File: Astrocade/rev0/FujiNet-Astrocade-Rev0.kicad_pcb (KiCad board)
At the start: 4 copper layers, 96 x 58 mm, 95 parts, among them J1 Astrocade_Cart_Edge_26, J2 microSD, J3 USB-C, Q2 BC847C, Q3 BC847C, SW1 RESET, SW2 BOOTSEL, SW3 RESET, SW4 BOOT, U1 RP2040, U2 ESP32-S3-WROOM-1-N16R8, U3 CP2102N-A02-GQFN28, U4 UMH3N, U5 AP63203WU, U6 W25Q16JVSSIQ, U7 SN74LVC245APW(data), U8 SN74LVC245APW(addr-lo), U9 SN74LVC245APW(addr-hi), Y1 12MHz

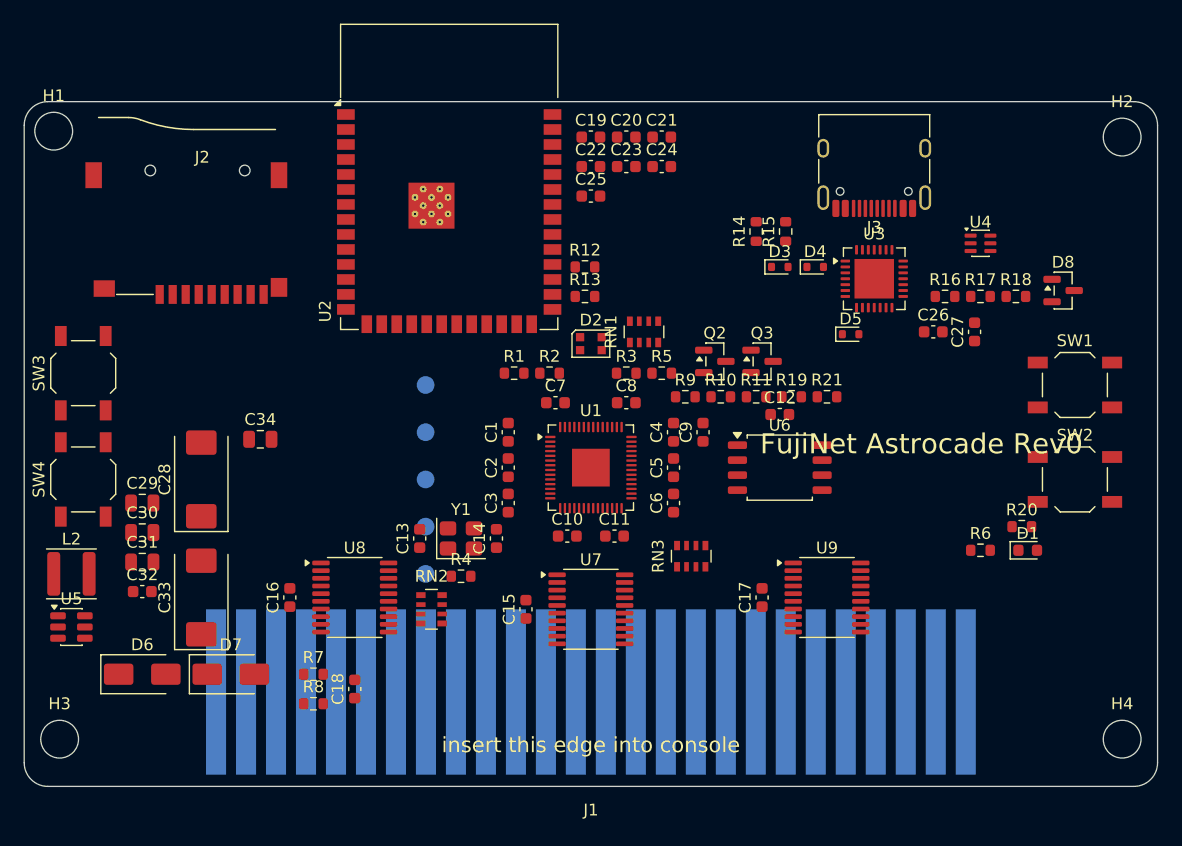
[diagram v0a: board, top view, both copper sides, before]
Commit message: Astrocade Rev0: redo on RP2354A + ESP32-S3, 6-layer, fully autorouted
Replaces the unrouted RP2040 + 3x LVC245 draft with an INTV-style board:
RP2354A straight on the 5V bus, ESP32-S3-WROOM-1-N16R8 as its USB host
(PICOBOOT reflash), USB-C/CP2102N, push-push microSD, WS2812B-2020-V6,
RESET/BOOTSEL/EN/BOOT buttons. Same cassette outline, lands and holes.

Everything is generated by tools/ (build_all.sh): design.py -> schematic,
placement + plane fan-out, Raspberry Pi's MIT regulator-corner graft,
Freerouting + A* finisher, netlist-vs-firmware check, JLCPCB BOM/CPL/gerbers.
ERC 0, DRC 0 errors / 0 unconnected / 0 parity, check_nets 174/174.

RUN/BOOTSEL from the S3 are direct 1k links (fnPicoUpdater drives them low;
an NPN driver would invert it). Shell openings come from the placement.

Co-Authored-By: Claude Opus 5.5 (1M context) <noreply@anthropic.com>
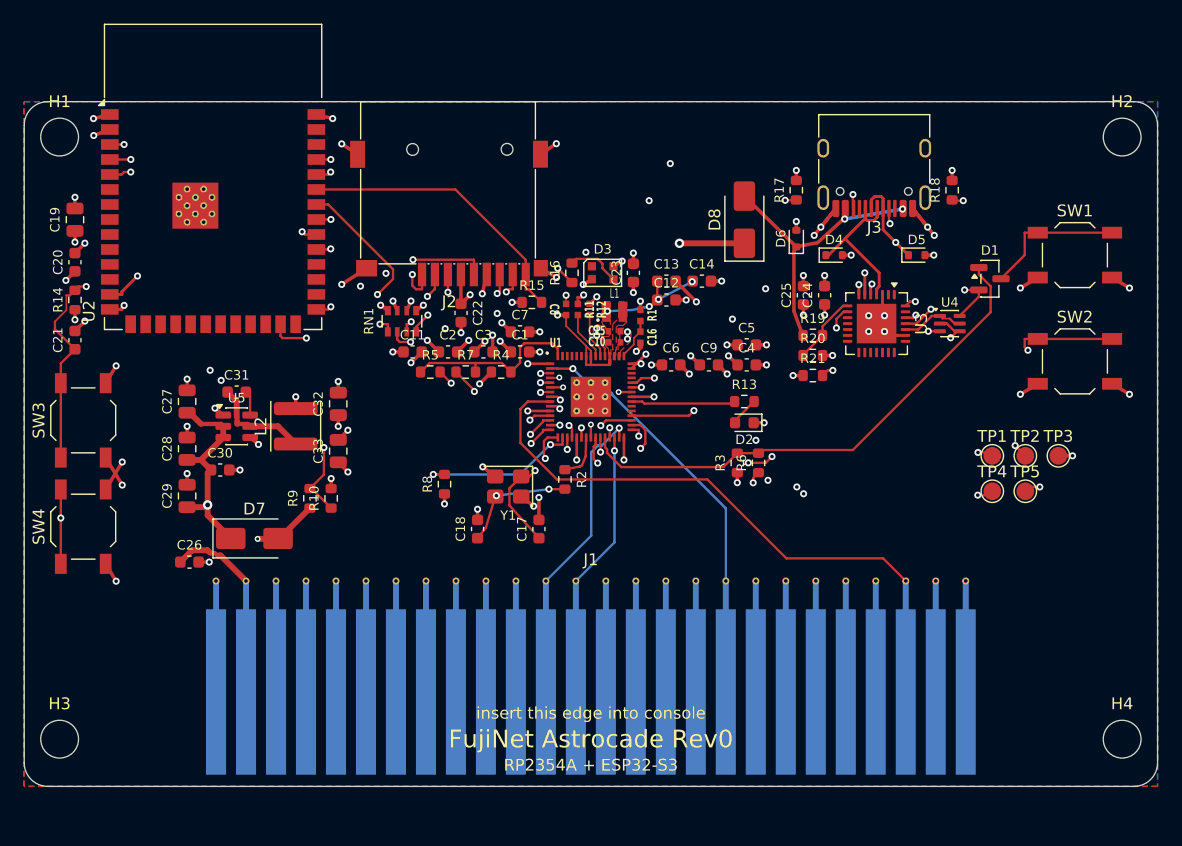
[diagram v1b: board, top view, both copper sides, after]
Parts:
- removed C34: 10uF, FujiNet-Astrocade:C_0805_2012Metric
- removed Q2, Q3: BC847C, FujiNet-Astrocade:SOT-23
- removed RN2, RN3: 100k, FujiNet-Astrocade:R_Array_Convex_4x0603
- removed U6: W25Q16JVSSIQ, FujiNet-Astrocade:SOIC-8_5.3x5.3mm_P1.27mm
- removed U7: SN74LVC245APW(data), FujiNet-Astrocade:TSSOP-20_4.4x6.5mm_P0.65mm
- removed U8: SN74LVC245APW(addr-lo), FujiNet-Astrocade:TSSOP-20_4.4x6.5mm_P0.65mm
- removed U9: SN74LVC245APW(addr-hi), FujiNet-Astrocade:TSSOP-20_4.4x6.5mm_P0.65mm
- added L1: 3.3uH, FujiNet-Astrocade:RPI_L_AOTA-B201610S3R3, F.Cu at (102.0, 47.8)
- C10: value 1uF -> 4.7uF; footprint FujiNet-Astrocade:C_0603_1608Metric -> FujiNet-Astrocade:RPI_C0402_wide
- C11: value 1uF -> 10uF
- C13, C14: value 27pF -> 100nF
- C15: value 100nF -> 4.7uF; footprint FujiNet-Astrocade:C_0603_1608Metric -> FujiNet-Astrocade:RPI_C0402_wide
- C16: value 100nF -> 4.7uF; footprint FujiNet-Astrocade:C_0603_1608Metric -> FujiNet-Astrocade:RPI_C0402
- C17, C18: value 100nF -> 15pF
- C19, C32: value 100nF -> 22uF; footprint FujiNet-Astrocade:C_0603_1608Metric -> FujiNet-Astrocade:C_0805_2012Metric
- C20: value 10uF -> 100nF
- C22: value 100nF -> 10uF
- C24, C9: value 1uF -> 100nF
- C25: value 100nF -> 4.7uF
- C27: value 4.7uF -> 22uF; footprint FujiNet-Astrocade:C_0603_1608Metric -> FujiNet-Astrocade:C_0805_2012Metric
- C28: value 470uF -> 22uF; footprint FujiNet-Astrocade:CP_EIA-7343-31_Kemet-D -> FujiNet-Astrocade:C_0805_2012Metric
- C29: value 10uF -> 22uF
- C30, C31: value 22uF -> 100nF; footprint FujiNet-Astrocade:C_0805_2012Metric -> FujiNet-Astrocade:C_0603_1608Metric
- C33: value 220uF -> 22uF; footprint FujiNet-Astrocade:CP_EIA-7343-31_Kemet-D -> FujiNet-Astrocade:C_0805_2012Metric
- C8: footprint FujiNet-Astrocade:C_0603_1608Metric -> FujiNet-Astrocade:RPI_C0402
- D1: value GREEN -> BAT54C; footprint FujiNet-Astrocade:LED_0603_1608Metric -> FujiNet-Astrocade:SOT-23
- D2: value WS2812B-2020 -> green; footprint FujiNet-Astrocade:LED_WS2812B-2020_PLCC4_2.0x2.0mm -> FujiNet-Astrocade:LED_0603_1608Metric
- D3: value ESD5Z5.0T1G -> WS2812B-2020-V6; footprint FujiNet-Astrocade:D_SOD-523 -> FujiNet-Astrocade:LED_WS2812B-2020_PLCC4_2.0x2.0mm
- D6: value SS34 -> ESD5Z5.0T1G; footprint FujiNet-Astrocade:D_SMA -> FujiNet-Astrocade:D_SOD-523
- D8: value BAT54C -> SS34; footprint FujiNet-Astrocade:SOT-23 -> FujiNet-Astrocade:D_SMA
- H1, H2, H3, H4: footprint MountingHole_3.2mm_NPTH -> FujiNet-Astrocade:MountingHole_3.2mm_NPTH
- J2: footprint FujiNet-Astrocade:microSD_SUNTECH_ST-TF-003A -> FujiNet-Astrocade:TF-SMD_TF-015
- R1: value 27R -> 33R; footprint FujiNet-Astrocade:R_0603_1608Metric -> FujiNet-Astrocade:RPI_R0402
- R10: value 100k -> 150k
- R11: value 10k -> 27R; footprint FujiNet-Astrocade:R_0603_1608Metric -> FujiNet-Astrocade:RPI_R0402
- R12: value 330R -> 27R; footprint FujiNet-Astrocade:R_0603_1608Metric -> FujiNet-Astrocade:RPI_R0402
- R13, R5: value 10k -> 1k
- R14, R15: value 5.1k -> 10k
- R16: value 22.1k -> 330R
- R17: value 47.5k -> 5.1k
- R18: value 10k -> 5.1k
- R19: value 100k -> 22k
- R2: value 27R -> 1k
- R20: value 1k -> 47k
- R4: value 1k -> 10k
- R7: value 100k -> 1k
- R8: value 100k -> 10k
- R9: value 10k -> 100k
- SW3: value RESET -> S3_RST
- SW4: value BOOT -> S3_BOOT
- TP1: value SWDIO -> SWCLK; moved to F.Cu
- TP2: value SWCLK -> SWDIO; moved to F.Cu
- TP3: moved to F.Cu
- TP4: value RP_DBG_TX -> SELFTEST; moved to F.Cu
- TP5: value SELFTEST -> DBG_TX; moved to F.Cu
- U1: value RP2040 -> RP2354A; footprint FujiNet-Astrocade:QFN-56-1EP_7x7mm_P0.4mm_EP3.2x3.2mm -> FujiNet-Astrocade:RPI_RP2350A_QFN60
- moved C27 67.0 mm to (65.8, 55.4)
- moved D6 66.6 mm to (117.4, 41.6), turned to 90 degrees
- moved C26 65.9 mm to (66.0, 69.0)
- moved R14 58.0 mm to (56.3, 46.8)
- moved TP3 53.6 mm to (139.6, 60.0)
- moved C21 52.6 mm to (56.3, 50.2), turned to 90 degrees
- moved TP5 51.3 mm to (136.8, 63.0)
- moved TP2 50.8 mm to (136.8, 60.0)
- moved TP1 48.4 mm to (134.0, 60.0)
- moved TP4 48.1 mm to (134.0, 63.0)
- moved C20 47.9 mm to (56.3, 43.6), turned to 90 degrees
- moved C19 44.3 mm to (56.3, 40.0), turned to 90 degrees
- moved C16 37.0 mm to (104.2, 50.0), turned to -90 degrees
- moved R10 34.1 mm to (78.0, 63.6), turned to 90 degrees
- moved R9 32.9 mm to (76.2, 63.6), turned to 90 degrees
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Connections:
- C10 pad 1: DVDD -> +3V3
- C11 pad 1: DVDD -> +3V3
- C12 pad 1: +3V3 -> DVDD
- C13 pad 1: XIN -> DVDD
- C14 pad 1: XOUT_Y -> DVDD
- C15 pad 1: +3V3 -> DVDD
- C16 pad 1: +3V3 -> VREG_AVDD
- C17 pad 1: +3V3 -> XIN
- C18 pad 1: VSENSE -> XOUT_Y
- C21 pad 1: +3V3 -> S3_EN
- C23 pad 1: VIN -> +3V3
- C24 pad 1: S3_EN -> +3V3
- C25 pad 1: S3_IO0 -> +3V3
- C26 pad 1: +3V3 -> +5V
- C27 pad 1: +3V3 -> VIN
- C30 pad 1: +3V3 -> VIN
- C31 pad 1: +3V3 -> BUCK_SW
- C31 pad 2: GND -> BUCK_BST
- C32 pad 1: BUCK_SW -> +3V3
- C32 pad 2: BUCK_BST -> GND
- D1 pad 1: GND -> RUN
- D1 pad 2: LED_A -> S3_EN
- D2 pad 1: unconnected-(D2-DOUT-Pad1) -> GND
- D2 pad 2: GND -> RP_LED_A
- D3 pad 1: UBRG_DP -> unconnected-(D3-DOUT-Pad1)
- D4 pad 1: UBRG_DM -> UBRG_DP
- D5 pad 1: VBUS -> UBRG_DM
- D6 pad 1: VIN -> VBUS
- D6 pad 2: +5V -> GND
- D7 pad 2: VBUS -> +5V
- D8 pad 1: RUN -> VIN
- D8 pad 2: S3_EN -> VBUS
- R1 pad 1: RP_USB_DP -> +3V3
- R1 pad 2: USB_DP -> VREG_AVDD
- R10 pad 1: Q2B -> VSENSE
- R11 pad 1: BOOTSEL_CTL -> USB_DP
- R11 pad 2: Q3B -> RP_USB_DP
- R12 pad 1: LED_STRIP -> USB_DM
- R12 pad 2: WS_DIN -> RP_USB_DM
- R13 pad 1: +3V3 -> RP_LED
- R13 pad 2: S3_EN -> RP_LED_A
- R14 pad 1: CC1 -> +3V3
- R14 pad 2: GND -> S3_EN
- R15 pad 1: CC2 -> +3V3
- R15 pad 2: GND -> SD_CD
- R16 pad 1: VBUS -> LED_STRIP
- R16 pad 2: VBUS_SNS -> WS_DIN
- R17 pad 1: VBUS_SNS -> CC1
- R18 pad 1: +3V3 -> CC2
- R18 pad 2: CP_RST -> GND
- R19 pad 1: Q3B -> VBUS
- R19 pad 2: GND -> VBUS_SNS
- R2 pad 1: RP_USB_DM -> XOUT
- R2 pad 2: USB_DM -> XOUT_Y
- R20 pad 1: QSPI_SS -> VBUS_SNS
- R20 pad 2: BOOTSEL_BTN -> GND
- R21 pad 1: B_TIE -> +3V3
- R21 pad 2: GND -> CP_RST
- R4 pad 1: XOUT_Y -> +3V3
- R4 pad 2: XOUT -> QSPI_SS
- R5 pad 1: +3V3 -> QSPI_SS
- R5 pad 2: QSPI_SS -> BOOTSEL_BTN
- R6 pad 1: RP_LED -> RUN_CTL
- R6 pad 2: LED_A -> RUN
- R7 pad 1: +5V -> BOOTSEL_CTL
- R7 pad 2: VSENSE -> QSPI_SS
- R8 pad 1: VSENSE -> +3V3
- R8 pad 2: GND -> CCS_N
- R9 pad 1: RUN_CTL -> +5V
- R9 pad 2: Q2B -> VSENSE
- TP1 pad 1: SWDIO -> SWCLK
- TP2 pad 1: SWCLK -> SWDIO
- TP4 pad 1: RP_DBG_TX -> SELFTEST
- TP5 pad 1: SELFTEST -> RP_DBG_TX
- U1 pad 10: +3V3 -> CA7
- U1 pad 11: RP_A8 -> +3V3
- U1 pad 12: RP_A9 -> CA8
- U1 pad 13: RP_A10 -> CA9
- U1 pad 14: RP_A11 -> CA10
- U1 pad 15: RP_A12 -> CA11
- U1 pad 16: RP_EN -> CA12
- U1 pad 17: RP_D0 -> CCS_N
- U1 pad 18: RP_D1 -> CD0
- U1 pad 19: GND -> CD1
- U1 pad 2: RP_A0 -> CA0
- U1 pad 20: XIN -> +3V3
- U1 pad 21: XOUT -> XIN
- U1 pad 22: +3V3 -> XOUT
- U1 pad 27: RP_D2 -> CD2
- U1 pad 28: RP_D3 -> CD3
- U1 pad 29: RP_D4 -> CD4
- U1 pad 3: RP_A1 -> CA1
- U1 pad 30: RP_D5 -> +3V3
- U1 pad 31: RP_D6 -> CD5
- U1 pad 32: RP_D7 -> CD6
- U1 pad 33: +3V3 -> CD7
- U1 pad 38: VSENSE -> +3V3
- U1 pad 39: RP_DBG_TX -> DVDD
- U1 pad 4: RP_A2 -> CA2
- U1 pad 40: unconnected-(U1-GPIO28/ADC2-Pad40) -> VSENSE
- U1 pad 41: unconnected-(U1-GPIO29/ADC3-Pad41) -> RP_DBG_TX
- U1 pad 42: +3V3 -> unconnected-(U1-GPIO28/ADC2-Pad42)
- U1 pad 43: +3V3 -> unconnected-(U1-GPIO29/ADC3-Pad43)
- U1 pad 45: DVDD -> +3V3
- U1 pad 46: RP_USB_DM -> VREG_AVDD
- U1 pad 47: RP_USB_DP -> GND
- U1 pad 48: +3V3 -> RP_LX
- U1 pad 5: RP_A3 -> CA3
- U1 pad 51: QSPI_SD3 -> RP_USB_DM
- U1 pad 52: QSPI_SCLK -> RP_USB_DP
- U1 pad 53: QSPI_SD0 -> +3V3
- U1 pad 54: QSPI_SD2 -> +3V3
- U1 pad 55: QSPI_SD1 -> unconnected-(U1-QSPI_SD3-Pad55)
- U1 pad 56: QSPI_SS -> unconnected-(U1-QSPI_SCLK-Pad56)
- U1 pad 57: GND -> unconnected-(U1-QSPI_SD0-Pad57)
- U1 pad 6: RP_A4 -> DVDD
- U1 pad 7: RP_A5 -> CA4
- U1 pad 8: RP_A6 -> CA5
- U1 pad 9: RP_A7 -> CA6
- U2 pad 35: unconnected-(U2-IO42-Pad35) -> SD_CD
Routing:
- net S3_EN: track 0.00 -> 112.0 mm, vias 0 -> 3
- net S3_IO0: track 0.00 -> 92.3 mm, vias 0 -> 3
- net GND: track 0.00 -> 87.3 mm, vias 0 -> 68
- net RUN_CTL: track 0.00 -> 79.3 mm, vias 0 -> 3
- net VIN: track 0.00 -> 74.7 mm, vias 0 -> 2
- net BOOTSEL_BTN: track 0.00 -> 61.8 mm, vias 0 -> 2
- net S3_TXD: track 0.00 -> 61.5 mm, vias 0 -> 4
- net S3_RXD: track 0.00 -> 59.5 mm, vias 0 -> 4
- net +3V3: track 0.00 -> 59.2 mm, vias 0 -> 42
- net USB_DM: track 0.00 -> 47.0 mm, vias 0 -> 3
- net BOOTSEL_CTL: track 0.00 -> 46.9 mm, vias 0 -> 3
- net CA4: track 0.00 -> 45.2 mm, vias 0 -> 1
- net RUN: track 0.00 -> 44.0 mm
- net USB_DP: track 0.00 -> 43.9 mm, vias 0 -> 4
- net CA6: track 0.00 -> 43.1 mm
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- added copper zone on F.Cu, net +3V3
- added copper zone on In4.Cu, net +3V3
- added copper zone on F.Cu, net DVDD
- added copper zone on In4.Cu, net DVDD
- added copper zone on B.Cu, net GND
- added copper zone on F.Cu, net GND
- added copper zone on In1.Cu, net GND
- added copper zone on F.Cu, net RP_LX
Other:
- copper layers 4 -> 6
- board text added: "RP2354A + ESP32-S3"
- board text added: "contacts: keep clean"
- board text removed: "contacts on this side - keep clean"
